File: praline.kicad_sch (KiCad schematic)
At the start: 0 parts

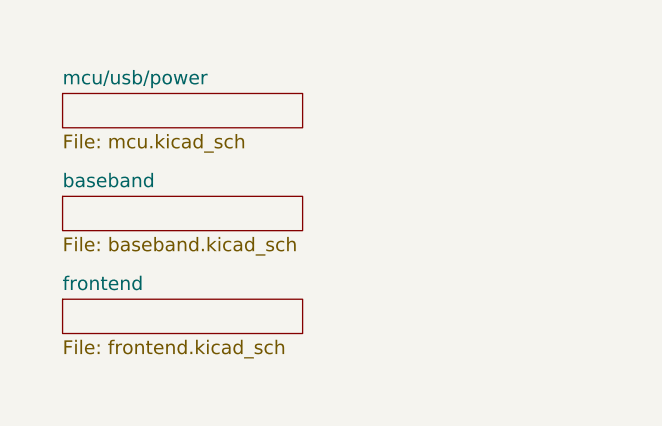
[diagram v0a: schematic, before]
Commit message: Replace CPLD U24 with FPGA U16
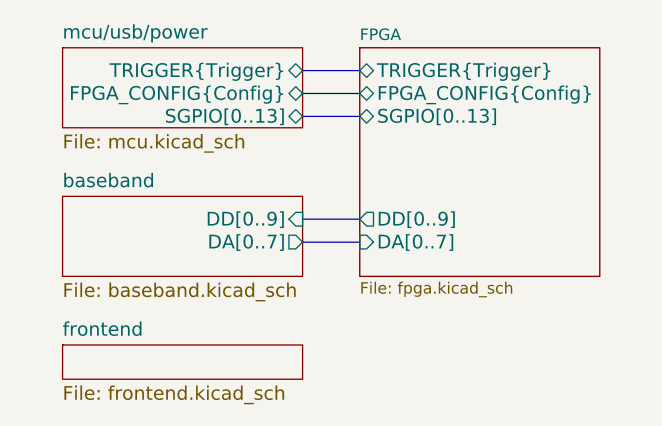
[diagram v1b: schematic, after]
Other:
- added sheet FPGA (fpga.kicad_sch)
- sheet baseband ports: added DA[0..7], DD[0..9]; removed none
- sheet mcu/usb/power ports: added FPGA_CONFIG{Config}, SGPIO[0..13], TRIGGER{Trigger}; removed none
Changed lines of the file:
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@@
 		(comment 1 "${LICENSE}")
 	)
-	(sheet
-		(at 64.77 60.96)
-		(size 26.67 3.81)
+	(bus
+		(pts
+			(xy 91.44 63.5) (xy 97.79 63.5)
+		)
+		(stroke
+			(width 0)
+			(type default)
+		)
+	)
+	(bus
+		(pts
+			(xy 91.44 60.96) (xy 97.79 60.96)
+		)
+		(stroke
+			(width 0)
+			(type default)
+		)
+	)
+	(bus
+		(pts
+			(xy 91.44 74.93) (xy 97.79 74.93)
+		)
+		(stroke
+			(width 0)
+			(type default)
+		)
+	)
+	(bus
+		(pts
+			(xy 91.44 77.47) (xy 97.79 77.47)
+		)
+		(stroke
+			(width 0)
+			(type default)
+		)
+	)
+	(bus
+		(pts
+			(xy 91.44 58.42) (xy 97.79 58.42)
+		)
+		(stroke
+			(width 0)
+			(type default)
+		)
+	)
+	(sheet
+		(at 64.77 55.88)
+		(size 26.67 8.89)
 		(fields_autoplaced yes)
 		(stroke
@@
 		)
 		(property "Sheetname" "mcu/usb/power"
-			(at 64.77 60.1214 0)
+			(at 64.77 55.0414 0)
 			(effects
 				(font
@@
 			)
 		)
+		(pin "SGPIO[0..13]" bidirectional
+			(at 91.44 63.5 0)
+			(effects
+				(font
+					(size 1.524 1.524)
+				)
+				(justify right)
+			)
+		)
+		(pin "FPGA_CONFIG{Config}" bidirectional
+			(at 91.44 60.96 0)
+			(effects
+				(font
+					(size 1.524 1.524)
+				)
+				(justify right)
+			)
+		)
+		(pin "TRIGGER{Trigger}" bidirectional
+			(at 91.44 58.42 0)
+			(effects
+				(font
+					(size 1.524 1.524)
+				)
+				(justify right)
+			)
+		)
 		(instances
 			(project "praline"
@@
 	(sheet
 		(at 64.77 72.39)
-		(size 26.67 3.81)
+		(size 26.67 8.89)
 		(fields_autoplaced yes)
 		(stroke
@@
 		)
 		(property "Sheetfile" "baseband.kicad_sch"
-			(at 64.77 76.8862 0)
-			(effects
-				(font
-					(size 1.524 1.524)
-				)
-				(justify left top)
+			(at 64.77 81.9662 0)
+			(effects
+				(font
+					(size 1.524 1.524)
+				)
+				(justify left top)
+			)
+		)
+		(pin "DD[0..9]" input
+			(at 91.44 74.93 0)
+			(effects
+				(font
+					(size 1.524 1.524)
+				)
+				(justify right)
+			)
+		)
+		(pin "DA[0..7]" output
+			(at 91.44 77.47 0)
+			(effects
+				(font
+					(size 1.524 1.524)
+				)
+				(justify right)
 			)
 		)
@@
 	)
 	(sheet
-		(at 64.77 83.82)
+		(at 64.77 88.9)
 		(size 26.67 3.81)
 		(fields_autoplaced yes)
@@
 		)
 		(property "Sheetname" "frontend"
-			(at 64.77 82.9814 0)
+			(at 64.77 88.0614 0)
 			(effects
 				(font
@@
 		)
 		(property "Sheetfile" "frontend.kicad_sch"
-			(at 64.77 88.3162 0)
+			(at 64.77 93.3962 0)
 			(effects
 				(font
@@
 				)
 			)
+		)
+	)
+	(sheet
+		(at 97.79 55.88)
+		(size 26.67 25.4)
+		(fields_autoplaced yes)
+		(stroke
+			(width 0.1524)
+			(type solid)
+		)
+		(fill
+			(color 0 0 0 0.0000)
+		)
+		(property "Sheetname" "FPGA"
+			(at 97.79 55.1684 0)
+			(effects
+				(font
+					(size 1.27 1.27)
+				)
+				(justify left bottom)
+			)
+		)
+		(property "Sheetfile" "fpga.kicad_sch"
+			(at 97.79 81.8646 0)
+			(effects
+				(font
+					(size 1.27 1.27)
+				)
+				(justify left top)
+			)
+		)
+		(pin "SGPIO[0..13]" bidirectional
+			(at 97.79 63.5 180)
+			(effects
+				(font
+					(size 1.524 1.524)
+				)
+				(justify left)
+			)
+		)
+		(pin "DD[0..9]" output
+			(at 97.79 74.93 180)
+			(effects
+				(font
+					(size 1.524 1.524)
+				)
+				(justify left)
+			)
+		)
+		(pin "DA[0..7]" input
+			(at 97.79 77.47 180)
+			(effects
+				(font
+					(size 1.524 1.524)
+				)
+				(justify left)
+			)
+		)
+		(pin "FPGA_CONFIG{Config}" bidirectional
+			(at 97.79 60.96 180)
+			(effects
+				(font
+					(size 1.524 1.524)
+				)
+				(justify left)
+			)
+		)
+		(pin "TRIGGER{Trigger}" bidirectional
+			(at 97.79 58.42 180)
+			(effects
+				(font
+					(size 1.524 1.524)
+				)
+				(justify left)
+			)
+		)
+		(instances
+			(project "praline"
+				(path "/dba4afc6-760f-46cb-a936-032b76448f03"
+					(page "5")
+				)
+			)

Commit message: Clean up radio layout
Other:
- added sheet ADC, DAC (adc-dac.kicad_sch)
- sheet baseband ports: added RXBB{IQ}, RXIF, TXBB{IQ}, TXIF; removed DA[0..7], DD[0..9]
- sheet frontend ports: added RXIF, TXIF; removed none
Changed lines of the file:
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@@
 	(generator "eeschema")
 	(generator_version "8.0")
-	(paper "User" 431.8 279.4)
+	(paper "A4")
 	(title_block
 		(title "${TITLE}")
@@
 	(bus
 		(pts
+			(xy 91.44 91.44) (xy 97.79 91.44)
+		)
+		(stroke
+			(width 0)
+			(type default)
+		)
+	)
+	(wire
+		(pts
+			(xy 124.46 91.44) (xy 134.62 91.44)
+		)
+		(stroke
+			(width 0)
+			(type default)
+		)
+	)
+	(bus
+		(pts
 			(xy 91.44 63.5) (xy 97.79 63.5)
 		)
@@
 		(pts
 			(xy 91.44 77.47) (xy 97.79 77.47)
+		)
+		(stroke
+			(width 0)
+			(type default)
+		)
+	)
+	(wire
+		(pts
+			(xy 124.46 93.98) (xy 134.62 93.98)
+		)
+		(stroke
+			(width 0)
+			(type default)
+		)
+	)
+	(bus
+		(pts
+			(xy 91.44 93.98) (xy 97.79 93.98)
 		)
 		(stroke
@@
 	)
 	(sheet
-		(at 64.77 72.39)
-		(size 26.67 8.89)
+		(at 97.79 88.9)
+		(size 26.67 7.62)
 		(fields_autoplaced yes)
 		(stroke
@@
 		)
 		(property "Sheetname" "baseband"
-			(at 64.77 71.5514 0)
+			(at 97.79 88.0614 0)
 			(effects
 				(font
@@
 		)
 		(property "Sheetfile" "baseband.kicad_sch"
-			(at 64.77 81.9662 0)
+			(at 97.79 97.2062 0)
 			(effects
 				(font
@@
 			)
 		)
-		(pin "DD[0..9]" input
-			(at 91.44 74.93 0)
-			(effects
-				(font
-					(size 1.524 1.524)
-				)
-				(justify right)
-			)
-		)
-		(pin "DA[0..7]" output
-			(at 91.44 77.47 0)
+		(pin "TXBB{IQ}" input
+			(at 97.79 93.98 180)
+			(effects
+				(font
+					(size 1.524 1.524)
+				)
+				(justify left)
+			)
+		)
+		(pin "RXBB{IQ}" output
+			(at 97.79 91.44 180)
+			(effects
+				(font
+					(size 1.524 1.524)
+				)
+				(justify left)
+			)
+		)
+		(pin "TXIF" output
+			(at 124.46 91.44 0)
+			(effects
+				(font
+					(size 1.524 1.524)
+				)
+				(justify right)
+			)
+		)
+		(pin "RXIF" input
+			(at 124.46 93.98 0)
 			(effects
 				(font
@@
 	)
 	(sheet
-		(at 64.77 88.9)
-		(size 26.67 3.81)
+		(at 134.62 88.9)
+		(size 26.67 7.62)
 		(fields_autoplaced yes)
 		(stroke
@@
 		)
 		(property "Sheetname" "frontend"
-			(at 64.77 88.0614 0)
+			(at 134.62 88.0614 0)
 			(effects
 				(font
@@
 		)
 		(property "Sheetfile" "frontend.kicad_sch"
-			(at 64.77 93.3962 0)
+			(at 134.62 97.2062 0)
 			(effects
 				(font
@@
 				)
 				(justify left top)
+			)
+		)
+		(pin "TXIF" input
+			(at 134.62 91.44 180)
+			(effects
+				(font
+					(size 1.524 1.524)
+				)
+				(justify left)
+			)
+		)
+		(pin "RXIF" output
+			(at 134.62 93.98 180)
+			(effects
+				(font
+					(size 1.524 1.524)
+				)
+				(justify left)
 			)
 		)
@@
 				)
 			)
+		)
+	)
+	(sheet
+		(at 64.77 72.39)
+		(size 26.67 27.94)
+		(fields_autoplaced yes)
+		(stroke
+			(width 0.1524)
+			(type solid)
+		)
+		(fill
+			(color 0 0 0 0.0000)
+		)
+		(property "Sheetname" "ADC, DAC"
+			(at 64.77 71.6784 0)
+			(effects
+				(font
+					(size 1.27 1.27)
+				)
+				(justify left bottom)
+			)
+		)
+		(property "Sheetfile" "adc-dac.kicad_sch"
+			(at 64.77 100.9146 0)
+			(effects
+				(font
+					(size 1.27 1.27)
+				)
+				(justify left top)
+			)
+		)
+		(pin "DA[0..7]" output
+			(at 91.44 77.47 0)
+			(effects
+				(font
+					(size 1.524 1.524)
+				)
+				(justify right)
+			)
+		)
+		(pin "DD[0..9]" input
+			(at 91.44 74.93 0)
+			(effects
+				(font
+					(size 1.524 1.524)
+				)
+				(justify right)
+			)
+		)
+		(pin "RXBB{IQ}" input
+			(at 91.44 91.44 0)
+			(effects
+				(font
+					(size 1.524 1.524)
+				)
+				(justify right)
+			)
+		)
+		(pin "TXBB{IQ}" output
+			(at 91.44 93.98 0)
+			(effects
+				(font
+					(size 1.524 1.524)
+				)
+				(justify right)
+			)
+		)
+		(instances
+			(project "praline"
+				(path "/dba4afc6-760f-46cb-a936-032b76448f03"
+					(page "7")
+				)
+			)

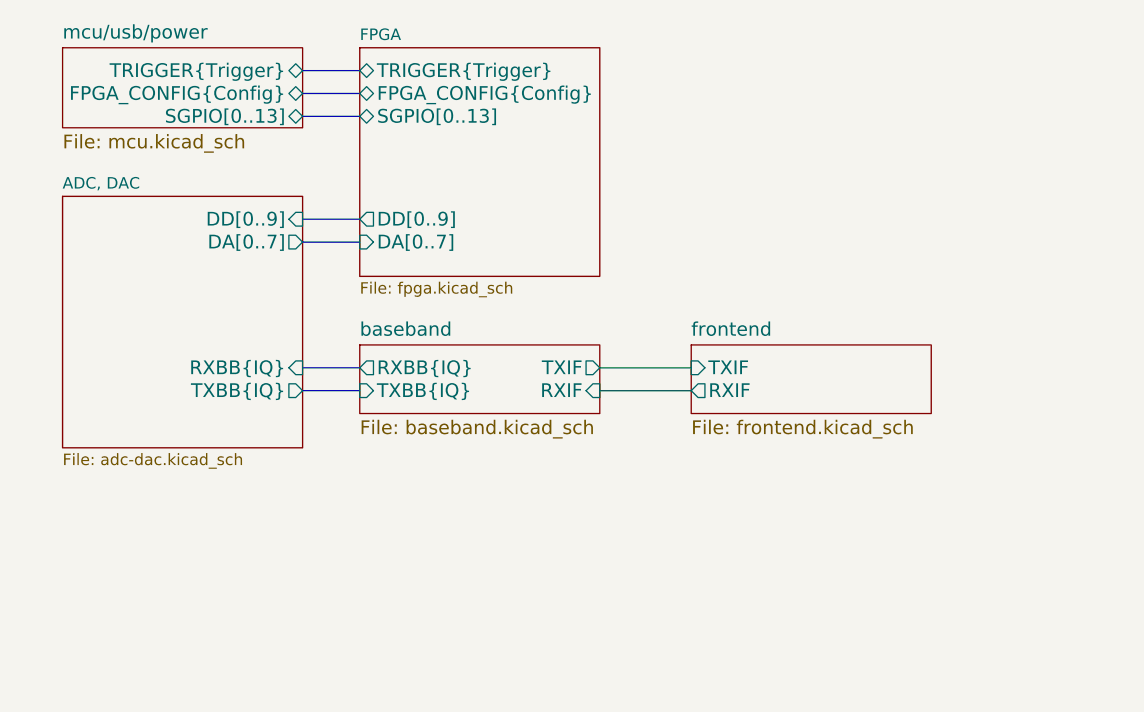
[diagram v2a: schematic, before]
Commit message: Make clock source termination consistent
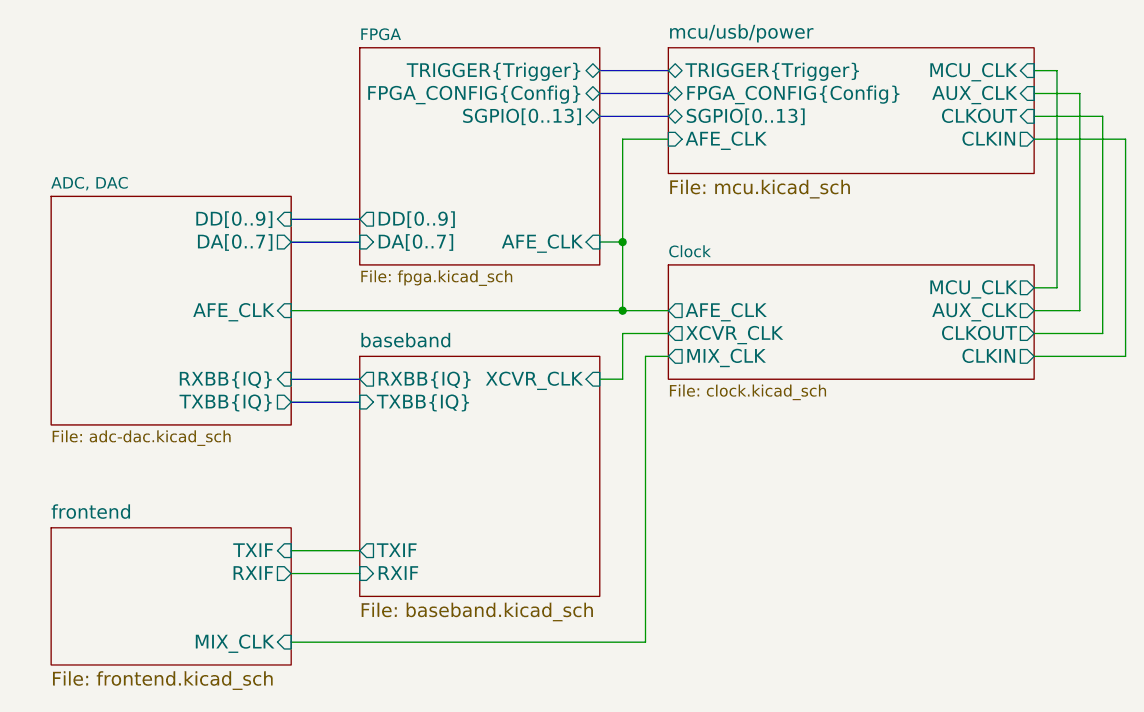
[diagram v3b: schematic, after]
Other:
- added sheet Clock (clock.kicad_sch)
- sheet ADC, DAC ports: added AFE_CLK; removed none
- sheet FPGA ports: added AFE_CLK; removed none
- sheet baseband ports: added XCVR_CLK; removed none
- sheet frontend ports: added MIX_CLK; removed none
- sheet mcu/usb/power ports: added AFE_CLK, AUX_CLK, CLKIN, CLKOUT, MCU_CLK; removed none

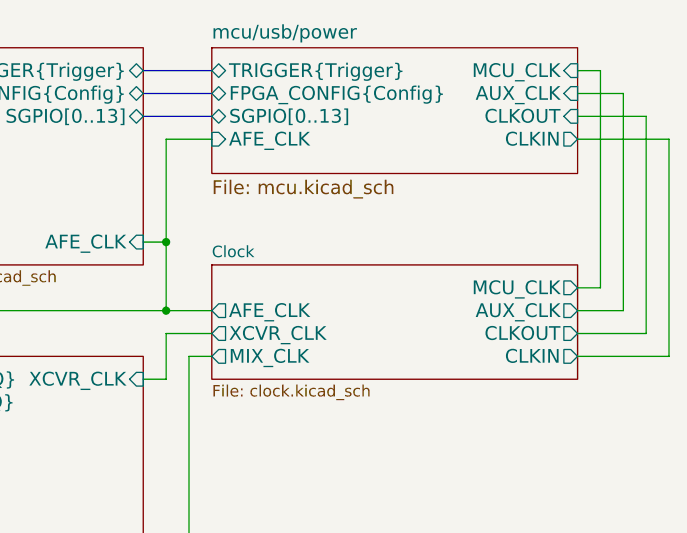
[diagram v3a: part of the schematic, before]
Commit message: Change microcontroller U23 to LPC4330FET180
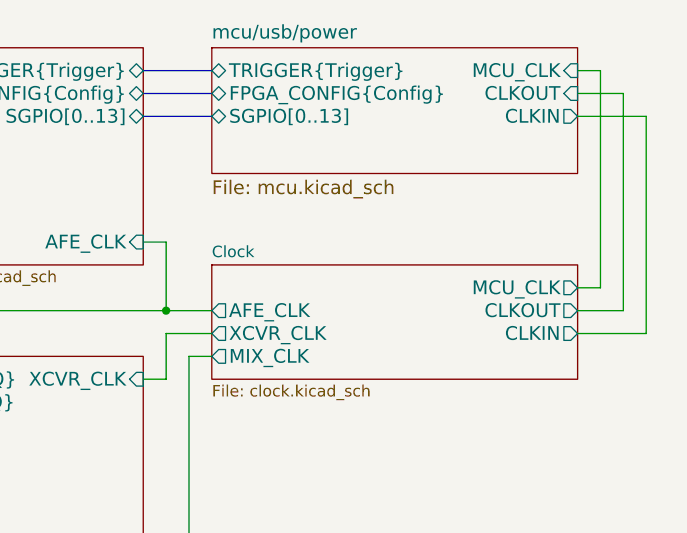
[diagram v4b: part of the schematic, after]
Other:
- sheet Clock ports: added none; removed AUX_CLK
- sheet mcu/usb/power ports: added none; removed AFE_CLK, AUX_CLK
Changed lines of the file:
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@@
 		(color 0 0 0 0)
 	)
-	(junction
-		(at 127 77.47)
-		(diameter 0)
-		(color 0 0 0 0)
-	)
-	(wire
-		(pts
-			(xy 182.88 66.04) (xy 182.88 90.17)
+	(wire
+		(pts
+			(xy 180.34 63.5) (xy 180.34 87.63)
+		)
+		(stroke
+			(width 0)
+			(type default)
+		)
+	)
+	(wire
+		(pts
+			(xy 177.8 85.09) (xy 172.72 85.09)
 		)
 		(stroke
@@
 		)
 	)
-	(wire
-		(pts
-			(xy 182.88 90.17) (xy 172.72 90.17)
-		)
-		(stroke
-			(width 0)
-			(type default)
-		)
-	)
-	(wire
-		(pts
-			(xy 127 77.47) (xy 127 66.04)
-		)
-		(stroke
-			(width 0)
-			(type default)
-		)
-	)
-	(wire
-		(pts
-			(xy 127 66.04) (xy 132.08 66.04)
-		)
-		(stroke
-			(width 0)
-			(type default)
-		)
-	)
-	(wire
-		(pts
-			(xy 177.8 85.09) (xy 172.72 85.09)
-		)
-		(stroke
-			(width 0)
-			(type default)
-		)
-	)
 	(bus
 		(pts
@@
 	(wire
 		(pts
-			(xy 180.34 63.5) (xy 180.34 87.63)
+			(xy 177.8 60.96) (xy 177.8 85.09)
+		)
+		(stroke
+			(width 0)
+			(type default)
+		)
+	)
+	(wire
+		(pts
+			(xy 172.72 60.96) (xy 177.8 60.96)
+		)
+		(stroke
+			(width 0)
+			(type default)
+		)
+	)
+	(wire
+		(pts
+			(xy 175.26 58.42) (xy 172.72 58.42)
+		)
+		(stroke
+			(width 0)
+			(type default)
+		)
+	)
+	(wire
+		(pts
+			(xy 172.72 82.55) (xy 175.26 82.55)
+		)
+		(stroke
+			(width 0)
+			(type default)
+		)
+	)
+	(wire
+		(pts
+			(xy 90.17 121.92) (xy 129.54 121.92)
 		)
 		(stroke
@@
 	(wire
 		(pts
-			(xy 175.26 58.42) (xy 172.72 58.42)
-		)
-		(stroke
-			(width 0)
-			(type default)
-		)
-	)
-	(wire
-		(pts
-			(xy 172.72 82.55) (xy 175.26 82.55)
-		)
-		(stroke
-			(width 0)
-			(type default)
-		)
-	)
-	(wire
-		(pts
-			(xy 90.17 121.92) (xy 129.54 121.92)
-		)
-		(stroke
-			(width 0)
-			(type default)
-		)
-	)
-	(wire
-		(pts
-			(xy 172.72 66.04) (xy 182.88 66.04)
-		)
-		(stroke
-			(width 0)
-			(type default)
-		)
-	)
-	(wire
-		(pts
 			(xy 90.17 114.3) (xy 97.79 114.3)
 		)
@@
 	(wire
 		(pts
-			(xy 177.8 60.96) (xy 177.8 85.09)
-		)
-		(stroke
-			(width 0)
-			(type default)
-		)
-	)
-	(wire
-		(pts
 			(xy 129.54 121.92) (xy 129.54 90.17)
 		)
@@
 		(pts
 			(xy 90.17 77.47) (xy 97.79 77.47)
-		)
-		(stroke
-			(width 0)
-			(type default)
-		)
-	)
-	(wire
-		(pts
-			(xy 172.72 60.96) (xy 177.8 60.96)
 		)
 		(stroke
@@
 		)
 		(pin "CLKOUT" input
+			(at 172.72 60.96 0)
+			(effects
+				(font
+					(size 1.524 1.524)
+				)
+				(justify right)
+			)
+		)
+		(pin "CLKIN" output
 			(at 172.72 63.5 0)
-			(effects
-				(font
-					(size 1.524 1.524)
-				)
-				(justify right)
-			)
-		)
-		(pin "CLKIN" output
-			(at 172.72 66.04 0)
-			(effects
-				(font
-					(size 1.524 1.524)
-				)
-				(justify right)
-			)
-		)
-		(pin "AUX_CLK" input
-			(at 172.72 60.96 0)
 			(effects
 				(font
@@
 				)
 				(justify right)
-			)
-		)
-		(pin "AFE_CLK" input
-			(at 132.08 66.04 180)
-			(effects
-				(font
-					(size 1.524 1.524)
-				)
-				(justify left)
 			)
 		)
@@
 			)
 		)
-		(pin "AUX_CLK" output
-			(at 172.72 85.09 0)
-			(effects
-				(font
-					(size 1.524 1.524)
-				)
-				(justify right)
-			)
-		)
 		(pin "MCU_CLK" output
 			(at 172.72 82.55 0)
@@
 		)
 		(pin "CLKOUT" output
-			(at 172.72 87.63 0)
+			(at 172.72 85.09 0)
 			(effects
 				(font
@@
 		)
 		(pin "CLKIN" output
-			(at 172.72 90.17 0)
-			(effects
-				(font
+			(at 172.72 87.63 0)
+			(effects
+				(font
